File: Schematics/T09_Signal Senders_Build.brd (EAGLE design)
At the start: 88.6 x 64.8 mm, 40 parts, among them IC1 7805TV, IC2 7805TV, IC3 ATMEGA328, SW1 UNIT_ID, X1 , Y2 16MHz

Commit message: Updated Board
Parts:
- moved C7 2.54 mm to (58.4, 54.6)
- moved IC2 1.27 mm to (54.6, 63.5)
- moved U$3 1.27 mm to (83.8, 61.0)
- moved U$4 1.27 mm to (5.08, 61.0)
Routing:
- net +3V3: track 78.1 -> 83.3 mm
- net +5V: track 165.0 -> 164.2 mm
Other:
- board size 88.6 x 64.8 mm -> 88.9 x 66 mm
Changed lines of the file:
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@@
 <?xml version="1.0" encoding="utf-8"?>
 <!DOCTYPE eagle SYSTEM "eagle.dtd">
-<eagle version="6.5.0">
+<eagle version="6.3">
 <drawing>
 <settings>
@@
 <setting verticaltext="up"/>
 </settings>
-<grid distance="0.05" unitdist="inch" unit="inch" style="lines" multiple="1" display="no" altdistance="0.025" altunitdist="inch" altunit="inch"/>
+<grid distance="0.1" unitdist="inch" unit="inch" style="lines" multiple="1" display="yes" altdistance="0.025" altunitdist="inch" altunit="inch"/>
 <layers>
 <layer number="1" name="Top" color="4" fill="1" visible="yes" active="yes"/>
@@
 <board>
 <plain>
-<wire x1="0" y1="0" x2="88.57" y2="0" width="0" layer="20"/>
-<wire x1="88.57" y1="0" x2="88.57" y2="64.76" width="0" layer="20"/>
-<wire x1="88.57" y1="64.76" x2="0" y2="64.76" width="0" layer="20"/>
-<wire x1="0" y1="64.76" x2="0" y2="0" width="0" layer="20"/>
+<wire x1="0" y1="0" x2="88.9" y2="0" width="0" layer="20"/>
+<wire x1="88.9" y1="0" x2="88.9" y2="66.04" width="0" layer="20"/>
+<wire x1="88.9" y1="66.04" x2="0" y2="66.04" width="0" layer="20"/>
+<wire x1="0" y1="66.04" x2="0" y2="0" width="0" layer="20"/>
 <text x="49.53" y="2.54" size="1.778" layer="25">T09 Signal Senders</text>
 <text x="67.31" y="2.54" size="1.778" layer="26" rot="MR0">Chris Klupenger
@@
 </element>
 <element name="LED4" library="led" package="LED3MM" value="NORTH" x="69.85" y="59.69" smashed="yes">
-<attribute name="VALUE" x="62.865" y="61.849" size="1.27" layer="27" ratio="10"/>
+<attribute name="VALUE" x="61.595" y="61.849" size="1.27" layer="27" ratio="10"/>
 </element>
 <element name="R1" library="rcl" package="M0805" value="1k" x="76.2" y="44.45" smashed="yes">
@@
 </element>
 <element name="S2" library="switch" package="M251" value="POWER" x="17.78" y="49.53" smashed="yes">
-<attribute name="NAME" x="12.7" y="52.705" size="1.778" layer="25"/>
-<attribute name="VALUE" x="12.7" y="44.45" size="1.778" layer="27"/>
+<attribute name="NAME" x="12.7" y="53.975" size="1.778" layer="25"/>
+<attribute name="VALUE" x="12.7" y="43.18" size="1.778" layer="27"/>
 </element>
 <element name="C4" library="rcl" package="C0805" value="22pF" x="74.93" y="6.35" smashed="yes">
@@
 <attribute name="NAME" x="16.51" y="12.7" size="1.27" layer="25"/>
 </element>
-<element name="IC2" library="linear" package="TO220V" value="7805TV" x="55.88" y="63.5" smashed="yes">
-<attribute name="NAME" x="50.8" y="57.4548" size="1.27" layer="25" ratio="10"/>
-<attribute name="VALUE" x="50.8" y="55.88" size="1.27" layer="27" ratio="10"/>
-</element>
-<element name="C7" library="rcl" package="C0805" value="10uF" x="60.96" y="54.61" smashed="yes" rot="R180">
-<attribute name="NAME" x="60.96" y="53.34" size="1.27" layer="25" rot="R180"/>
+<element name="IC2" library="linear" package="TO220V" value="7805TV" x="54.61" y="63.5" smashed="yes">
+<attribute name="NAME" x="49.53" y="57.4548" size="1.27" layer="25" ratio="10"/>
+<attribute name="VALUE" x="49.53" y="55.88" size="1.27" layer="27" ratio="10"/>
+</element>
+<element name="C7" library="rcl" package="C0805" value="10uF" x="58.42" y="54.61" smashed="yes" rot="R180">
+<attribute name="NAME" x="58.42" y="53.34" size="1.27" layer="25" rot="R180"/>
 </element>
 <element name="JP4" library="pinhead" package="1X02" value=" " x="69.85" y="25.4" smashed="yes">
@@
 <element name="U$1" library="holes" package="3,2" value="" x="5.08" y="5.08" smashed="yes"/>
 <element name="U$2" library="holes" package="3,2" value="" x="83.82" y="5.08" smashed="yes"/>
-<element name="U$3" library="holes" package="3,2" value="" x="83.82" y="59.69" smashed="yes"/>
-<element name="U$4" library="holes" package="3,2" value="" x="5.08" y="59.69" smashed="yes"/>
+<element name="U$3" library="holes" package="3,2" value="" x="83.82" y="60.96" smashed="yes"/>
+<element name="U$4" library="holes" package="3,2" value="" x="5.08" y="60.96" smashed="yes"/>
 <element name="SV2" library="con-lstb" package="MA04-1" value=" " x="31.75" y="27.94" smashed="yes" rot="R270">
 <attribute name="OC_NEWARK" value="unknown" x="31.75" y="27.94" size="1.778" layer="27" rot="R270" display="off"/>
@@
 <contactref element="SV1" pad="6"/>
 <polygon width="0.4064" layer="1">
-<vertex x="0" y="64.77"/>
-<vertex x="88.9" y="64.77"/>
+<vertex x="0" y="66.04"/>
+<vertex x="88.9" y="66.04"/>
 <vertex x="88.9" y="0"/>
 <vertex x="0" y="0"/>
 </polygon>
 <polygon width="0.4064" layer="16">
-<vertex x="0" y="64.77"/>
+<vertex x="0" y="66.04"/>
 <vertex x="0" y="0"/>
 <vertex x="88.9" y="0"/>
-<vertex x="88.9" y="64.77"/>
+<vertex x="88.9" y="66.04"/>
 </polygon>
 </signal>
@@
 <wire x1="37.592" y1="52.07" x2="37.592" y2="57.658" width="0.3048" layer="1"/>
 <wire x1="47.244" y1="54.864" x2="49.53" y2="57.15" width="0.3048" layer="1"/>
-<wire x1="49.53" y1="57.15" x2="53.34" y2="60.96" width="0.3048" layer="1"/>
+<wire x1="49.53" y1="57.15" x2="52.07" y2="60.96" width="0.3048" layer="1"/>
 <wire x1="45.466" y1="54.864" x2="47.244" y2="54.864" width="0.3048" layer="1"/>
 <wire x1="45.466" y1="54.61" x2="45.466" y2="54.864" width="0.3048" layer="1"/>
@@
 <contactref element="JP1" pad="2"/>
 <wire x1="61.722" y1="56.388" x2="61.722" y2="54.61" width="0.3048" layer="1"/>
-<wire x1="58.42" y1="59.69" x2="61.722" y2="56.388" width="0.3048" layer="1"/>
-<wire x1="58.42" y1="60.96" x2="58.42" y2="59.69" width="0.3048" layer="1"/>
-<wire x1="61.722" y1="54.61" x2="61.91" y2="54.61" width="0.3048" layer="1"/>
+<wire x1="57.15" y1="60.96" x2="61.722" y2="56.388" width="0.3048" layer="1"/>
+<wire x1="61.722" y1="54.61" x2="59.37" y2="54.61" width="0.3048" layer="1"/>
 <wire x1="74.168" y1="8.89" x2="74.168" y2="6.604" width="0.3048" layer="1"/>
 <wire x1="74.168" y1="6.604" x2="74.168" y2="6.35" width="0.3048" layer="1"/>
@@
 <wire x1="68.834" y1="6.604" x2="60.96" y2="14.478" width="0.3048" layer="1"/>
 <wire x1="74.168" y1="6.604" x2="68.834" y2="6.604" width="0.3048" layer="1"/>
-<wire x1="61.976" y1="54.61" x2="61.91" y2="54.61" width="0.3048" layer="1"/>
+<wire x1="61.976" y1="54.61" x2="59.37" y2="54.61" width="0.3048" layer="1"/>
 <wire x1="74.168" y1="6.604" x2="73.98" y2="6.35" width="0.3048" layer="1"/>
 </signal>

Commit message: Andrew's fixes from office hours
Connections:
- removed net N$17: IC3.12
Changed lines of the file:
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@@
 <?xml version="1.0" encoding="utf-8"?>
 <!DOCTYPE eagle SYSTEM "eagle.dtd">
-<eagle version="6.3">
+<eagle version="6.5.0">
 <drawing>
 <settings>
@@
 <layer number="27" name="tValues" color="7" fill="1" visible="yes" active="yes"/>
 <layer number="28" name="bValues" color="7" fill="1" visible="yes" active="yes"/>
-<layer number="29" name="tStop" color="7" fill="3" visible="yes" active="yes"/>
-<layer number="30" name="bStop" color="7" fill="6" visible="yes" active="yes"/>
-<layer number="31" name="tCream" color="7" fill="4" visible="yes" active="yes"/>
+<layer number="29" name="tStop" color="7" fill="3" visible="no" active="yes"/>
+<layer number="30" name="bStop" color="7" fill="6" visible="no" active="yes"/>
+<layer number="31" name="tCream" color="7" fill="4" visible="no" active="yes"/>
 <layer number="32" name="bCream" color="7" fill="5" visible="yes" active="yes"/>
 <layer number="33" name="tFinish" color="6" fill="3" visible="yes" active="yes"/>
@@
 <layer number="42" name="bRestrict" color="1" fill="10" visible="yes" active="yes"/>
 <layer number="43" name="vRestrict" color="2" fill="10" visible="yes" active="yes"/>
-<layer number="44" name="Drills" color="7" fill="1" visible="yes" active="yes"/>
+<layer number="44" name="Drills" color="7" fill="1" visible="no" active="yes"/>
 <layer number="45" name="Holes" color="7" fill="1" visible="yes" active="yes"/>
 <layer number="46" name="Milling" color="3" fill="1" visible="yes" active="yes"/>
@@
 <contactref element="C3" pad="2"/>
 <contactref element="SV1" pad="6"/>
-<polygon width="0.4064" layer="1">
+<polygon width="0.4064" layer="1" isolate="0.254">
 <vertex x="0" y="66.04"/>
 <vertex x="88.9" y="66.04"/>
@@
 <vertex x="0" y="0"/>
 </polygon>
-<polygon width="0.4064" layer="16">
+<polygon width="0.4064" layer="16" isolate="0.254">
 <vertex x="0" y="66.04"/>
 <vertex x="0" y="0"/>
@@
 <vertex x="88.9" y="66.04"/>
 </polygon>
+<via x="10.16" y="10.16" extent="1-16" drill="0.6"/>
 </signal>
 <signal name="+5V">
@@
 <via x="34.29" y="20.32" extent="1-16" drill="0.6096"/>
 </signal>
-<signal name="N$17">
-<contactref element="IC3" pad="12"/>
-</signal>
 <signal name="+3V3">
 <contactref element="IC2" pad="3"/>
@@
 <via x="6.35" y="39.37" extent="1-16" drill="0.6"/>
 </signal>
-<signal name="N$13">
-<via x="10.16" y="10.16" extent="1-16" drill="0.6"/>
-</signal>
 <signal name="N$19">

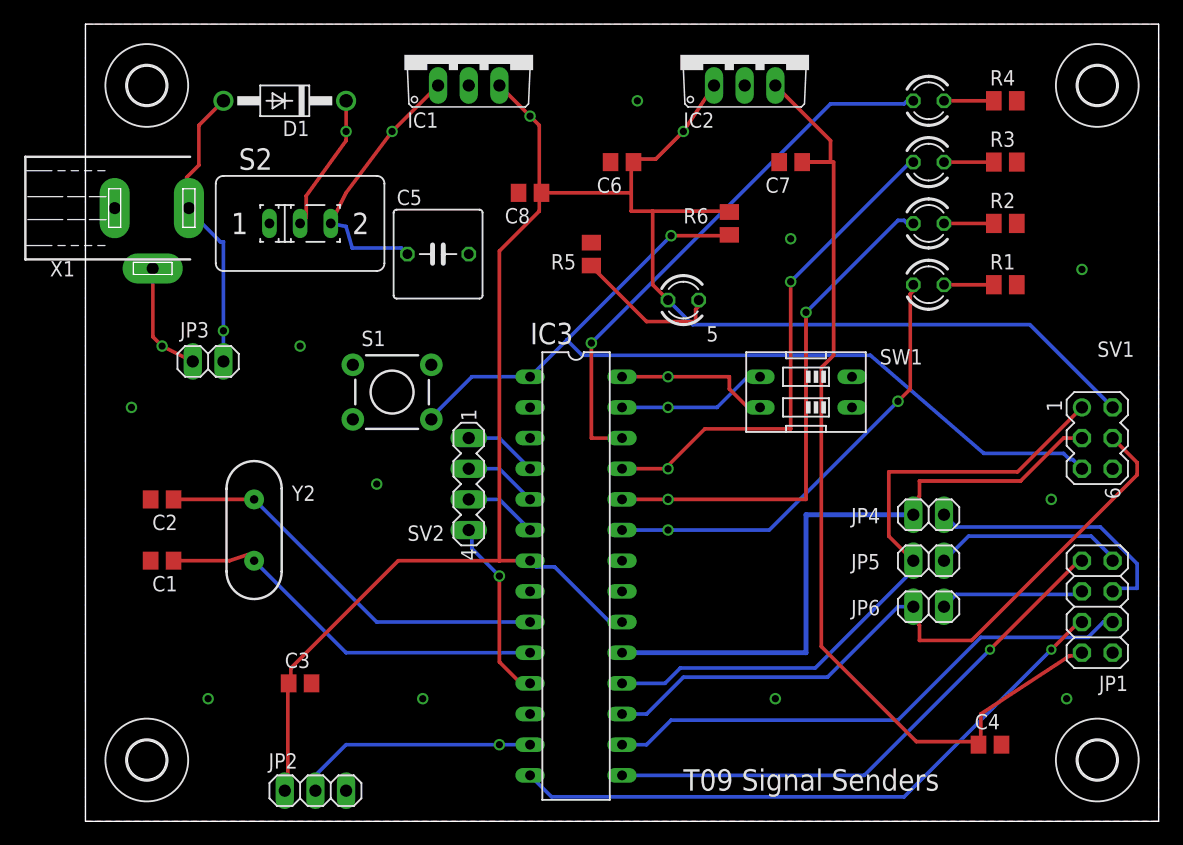
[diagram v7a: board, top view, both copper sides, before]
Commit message: Fixes as per Andrews recommendations
vcc lines larger, gnd vias, move crystal and bypass caps, add diode to
battery, version, names
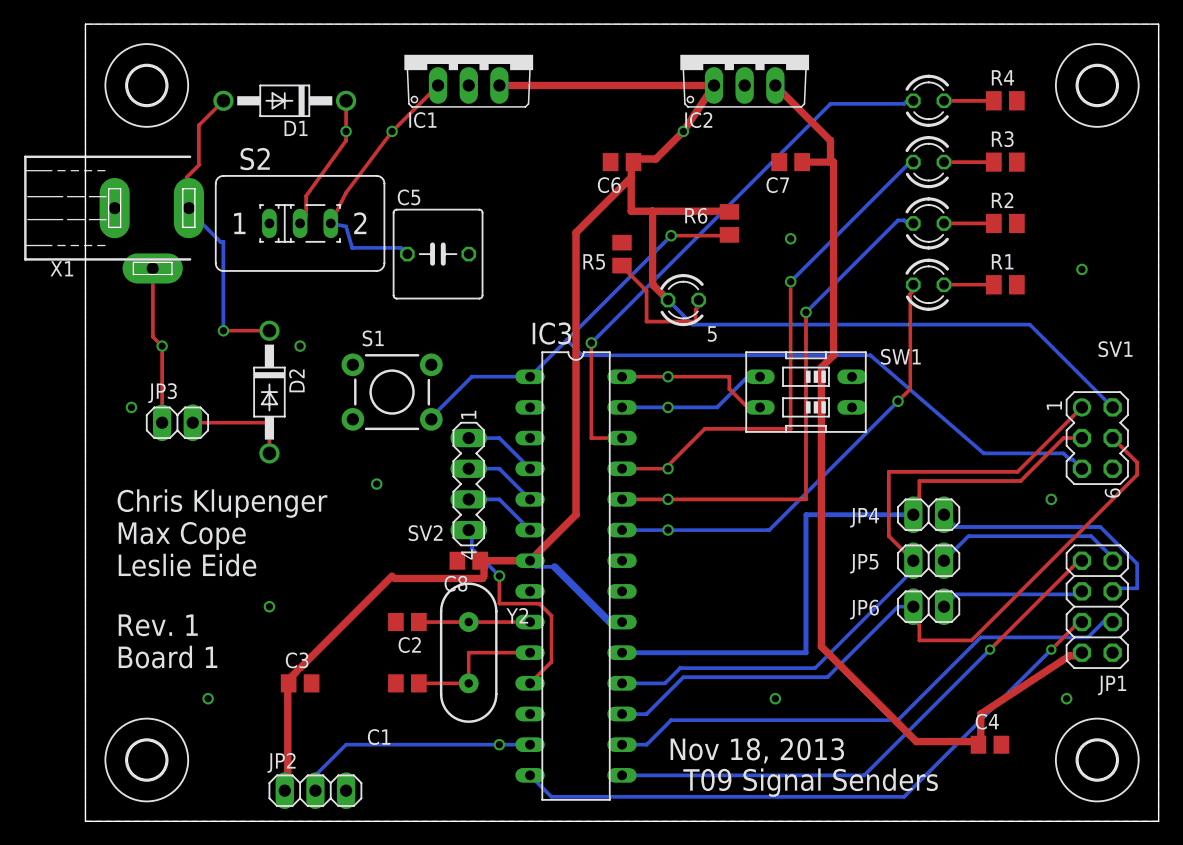
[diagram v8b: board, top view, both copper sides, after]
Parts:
- added D2: 1N4004, diode:DO41-10
- moved C8 30.9 mm to (31.8, 21.6)
- moved C1 22.7 mm to (26.7, 11.4)
- moved C2 22.7 mm to (26.7, 16.5)
- moved Y2 20.5 mm to (31.8, 14.0)
- moved JP3 5.68 mm to (7.62, 33.0)
- moved R5 2.54 mm to (44.5, 47.0)
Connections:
- new net N$13: D2.A, JP3.1
- net +9V: now also D2.C; no longer JP3.1
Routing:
- net N$3: track 33.7 -> 9.21 mm
- net N$2: track 33.0 -> 11.7 mm
- net N$13: track 0.00 -> 8.89 mm
- net +5V: track 164.2 -> 168.7 mm, vias 2 -> 1
- net N$16: track 15.5 -> 19.6 mm
- net N$14: track 9.59 -> 13.1 mm
- net +9V: track 24.6 -> 25.9 mm
- net N$18: track 12.5 -> 11.4 mm
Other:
- board text added: "Nov 18, 2013"
- board text added: "Rev. 1 Board 1"
